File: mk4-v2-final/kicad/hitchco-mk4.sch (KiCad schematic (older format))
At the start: 25 parts, among them J1 Screw_Terminal_01x10, J10 Conn_02x03_Counter_Clockwise, J12 Conn_02x03_Counter_Clockwise, J13 Conn_02x03_Counter_Clockwise, J15 Conn_02x03_Counter_Clockwise, J16 Conn_02x03_Counter_Clockwise, J18 Conn_02x03_Counter_Clockwise, J19 Conn_02x03_Counter_Clockwise, J2 Screw_Terminal_01x10, J21 Conn_02x03_Counter_Clockwise, J22 Conn_02x03_Counter_Clockwise, J24 Conn_02x03_Counter_Clockwise, J25 Conn_02x03_Counter_Clockwise, J26 Conn_02x03_Counter_Clockwise, J27 Conn_02x03_Counter_Clockwise, J28 Conn_02x03_Counter_Clockwise, J30 Conn_02x03_Counter_Clockwise, J4 Screw_Terminal_01x10, J5 Conn_02x03_Counter_Clockwise, J6 Screw_Terminal_01x10, J7 Conn_02x03_Counter_Clockwise, J8 Conn_02x03_Counter_Clockwise

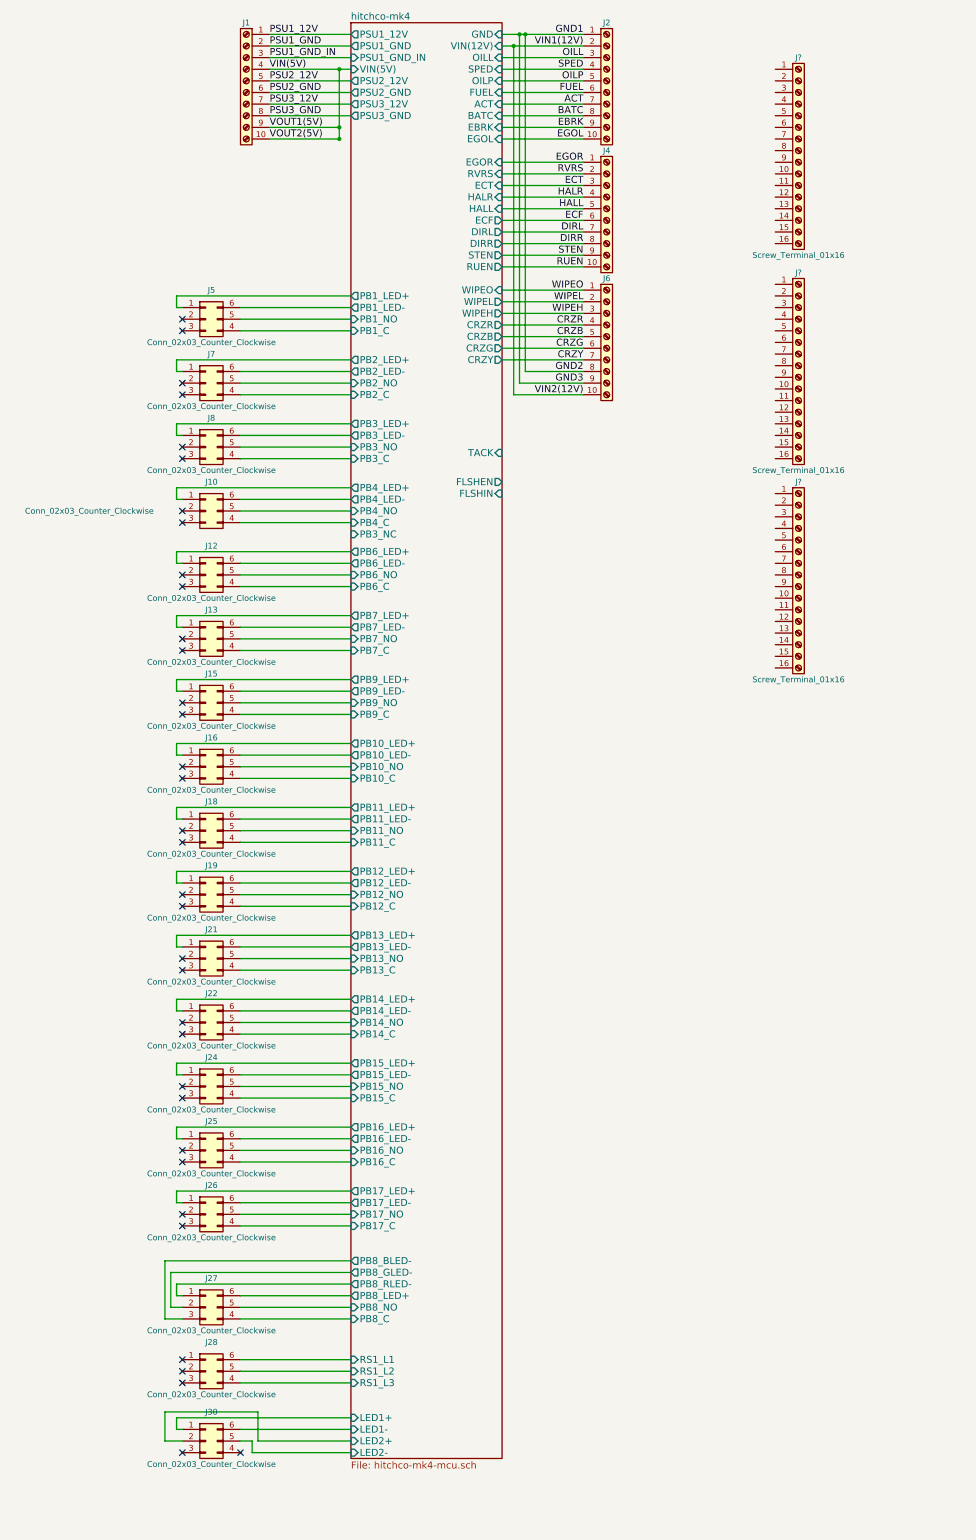
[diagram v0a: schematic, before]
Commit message: got most of the screw terminals planned out in schem
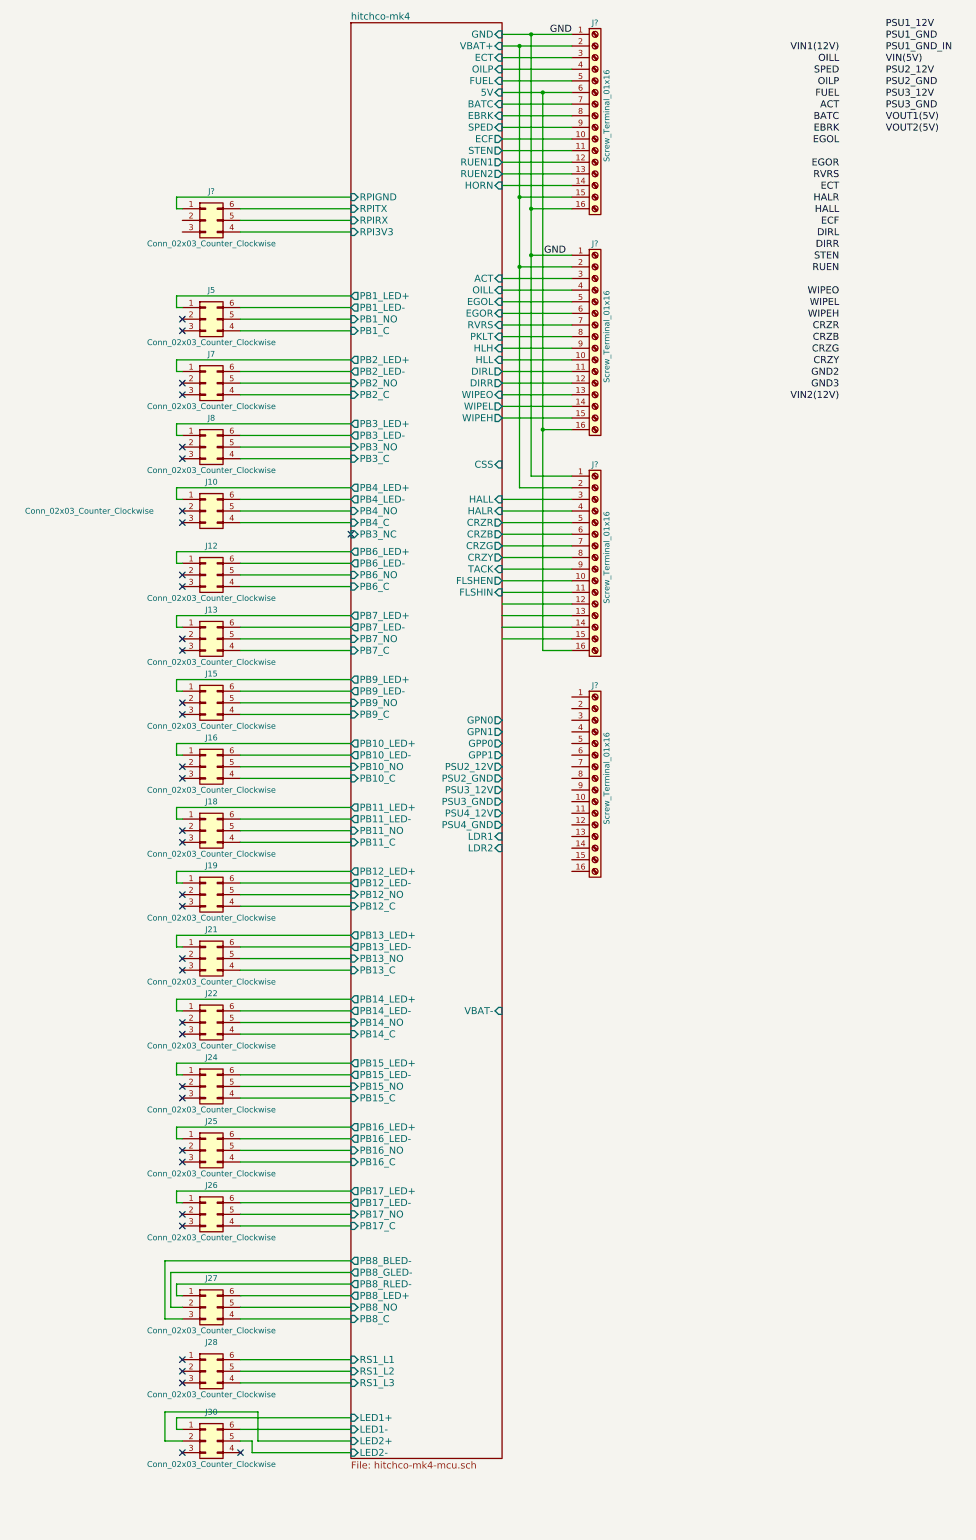
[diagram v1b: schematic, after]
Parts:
- removed J1, J2, J4, J6: Screw_Terminal_01x10, TerminalBlocks_Phoenix:TerminalBlock_Phoenix_MKDS1.5-10pol, symbol Screw_Terminal_01x10
- added J?: Conn_02x03_Counter_Clockwise, Socket_Strips:Socket_Strip_Straight_2x03_Pitch2.54mm, symbol Conn_02x03_Counter_Clockwise
- added J?: Screw_Terminal_01x16, symbol Screw_Terminal_01x16
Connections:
- net hitchco-mk4/FLSHEN: now also J?.10 (Pin_10)
- net hitchco-mk4/FLSHIN: now also J?.11 (Pin_11)
- net hitchco-mk4/TACK: now also J?.9 (Pin_9)
- net GND: now reaches J?.1 (Pin_1)
- net GND: now also J?.1 (Pin_1), J?.1 (Pin_1), J?.16 (Pin_16)
- net hitchco-mk4/ECF: now reaches J?.10 (Pin_10)
- net hitchco-mk4/STEN: now reaches J?.11 (Pin_11)
- net hitchco-mk4/RUEN1: now reaches J?.12 (Pin_12)
- net hitchco-mk4/RUEN2: now reaches J?.13 (Pin_13)
- net hitchco-mk4/HORN: now reaches J?.14 (Pin_14)
- net hitchco-mk4/VBAT+: now reaches J?.15 (Pin_15)
- net hitchco-mk4/VBAT+: now also J?.2 (Pin_2), J?.2 (Pin_2), J?.2 (Pin_2)
- net hitchco-mk4/ECT: now reaches J?.3 (Pin_3)
- net hitchco-mk4/OILP: now reaches J?.4 (Pin_4)
- net hitchco-mk4/FUEL: now reaches J?.5 (Pin_5)
- net hitchco-mk4/5V: now reaches J?.6 (Pin_6)
- net hitchco-mk4/5V: now also J?.16 (Pin_16), J?.16 (Pin_16)
- net hitchco-mk4/BATC: now reaches J?.7 (Pin_7)
- net hitchco-mk4/EBRK: now reaches J?.8 (Pin_8)
- net hitchco-mk4/SPED: now reaches J?.9 (Pin_9)
- net hitchco-mk4/HLL: now reaches J?.10 (Pin_10)
- net hitchco-mk4/DIRL: now reaches J?.11 (Pin_11)
- net hitchco-mk4/DIRR: now reaches J?.12 (Pin_12)
- net hitchco-mk4/WIPEO: now reaches J?.13 (Pin_13)
- net hitchco-mk4/WIPEL: now reaches J?.14 (Pin_14)
- net hitchco-mk4/WIPEH: now reaches J?.15 (Pin_15)
- net hitchco-mk4/ACT: now reaches J?.3 (Pin_3)
- net hitchco-mk4/OILL: now reaches J?.4 (Pin_4)
- net hitchco-mk4/EGOL: now reaches J?.5 (Pin_5)
- net hitchco-mk4/EGOR: now reaches J?.6 (Pin_6)
- net hitchco-mk4/RVRS: now reaches J?.7 (Pin_7)
- net hitchco-mk4/PKLT: now reaches J?.8 (Pin_8)
- net hitchco-mk4/HLH: now reaches J?.9 (Pin_9)
- net hitchco-mk4/HALL: now reaches J?.3 (Pin_3)
- net hitchco-mk4/HALR: now reaches J?.4 (Pin_4)
- net hitchco-mk4/CRZR: now reaches J?.5 (Pin_5)
- net hitchco-mk4/CRZB: now reaches J?.6 (Pin_6)
- net hitchco-mk4/CRZG: now reaches J?.7 (Pin_7)
- net hitchco-mk4/CRZY: now reaches J?.8 (Pin_8)
- new net hitchco-mk4/RPI3V3: J?.4 (Pin_4)
- new net hitchco-mk4/RPIGND: J?.1 (Pin_1)
- new net hitchco-mk4/RPIRX: J?.5 (Pin_5)
- new net hitchco-mk4/RPITX: J?.6 (Pin_6)
- no-connect marks 35 -> 36
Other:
- moved on the sheet: J?

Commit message: added headnight diodes, I don't think software control of them is going to be possible
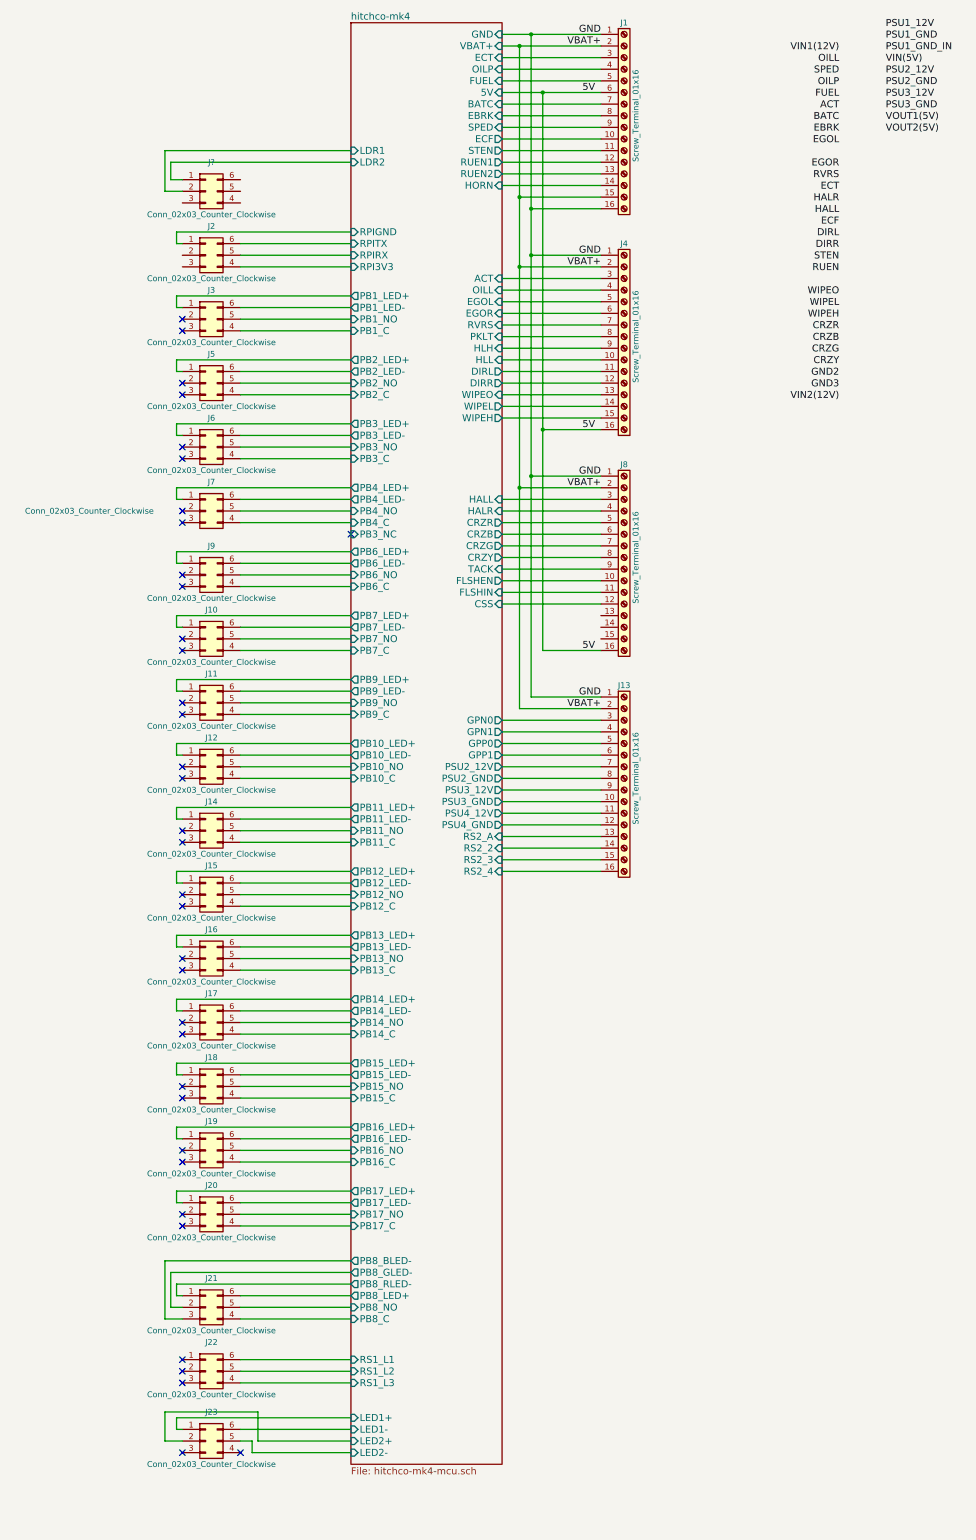
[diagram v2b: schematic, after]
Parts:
- added J?: Conn_02x03_Counter_Clockwise, Socket_Strips:Socket_Strip_Straight_2x03_Pitch2.54mm, symbol Conn_02x03_Counter_Clockwise
- J1, J13, J4, J8: renamed from J?; footprint (none) -> TerminalBlocks_Phoenix:TerminalBlock_Phoenix_MKDS1.5-16pol
- gave numbers to parts that had none: 1
- renumbered J13 to J10, J15 to J11, J16 to J12, J18 to J14, J19 to J15, J21 to J16, J22 to J17, J24 to J18, J25 to J19, J26 to J20, J27 to J21, J28 to J22, J30 to J23, J5 to J3, J7 to J5, J8 to J6, J10 to J7, J12 to J9
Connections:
- net hitchco-mk4/VBAT+ is gone; now on net VBAT+: J1.15 (Pin_15), J1.2 (Pin_2), J4.2 (Pin_2), J8.2 (Pin_2)
- net GND: now also J13.1 (Pin_1)
- net hitchco-mk4/CSS: now also J8.12 (Pin_12)
- net hitchco-mk4/GPN0: now also J13.3 (Pin_3)
- net hitchco-mk4/GPN1: now also J13.4 (Pin_4)
- net hitchco-mk4/GPP0: now also J13.5 (Pin_5)
- net hitchco-mk4/GPP1: now also J13.6 (Pin_6)
- net hitchco-mk4/LDR1: now also J?.2 (Pin_2)
- net hitchco-mk4/LDR2: now also J?.1 (Pin_1)
- net hitchco-mk4/PSU2_12V: now also J13.7 (Pin_7)
- net hitchco-mk4/PSU2_GND: now also J13.8 (Pin_8)
- net hitchco-mk4/PSU3_12V: now also J13.9 (Pin_9)
- net hitchco-mk4/PSU3_GND: now also J13.10 (Pin_10)
- net hitchco-mk4/PSU4_12V: now also J13.11 (Pin_11)
- net hitchco-mk4/PSU4_GND: now also J13.12 (Pin_12)
- net hitchco-mk4/RS2_A: now reaches J13.13 (Pin_13)
- net hitchco-mk4/RS2_2: now reaches J13.14 (Pin_14)
- net hitchco-mk4/RS2_3: now reaches J13.15 (Pin_15)
- net hitchco-mk4/RS2_4: now reaches J13.16 (Pin_16)
- net VBAT+: now reaches J13.2 (Pin_2)
- net hitchco-mk4/5V renamed 5V
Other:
- moved on the sheet: J1, J13, J2, J4, J8

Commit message: schematic is done, footprint association and netlist are also done
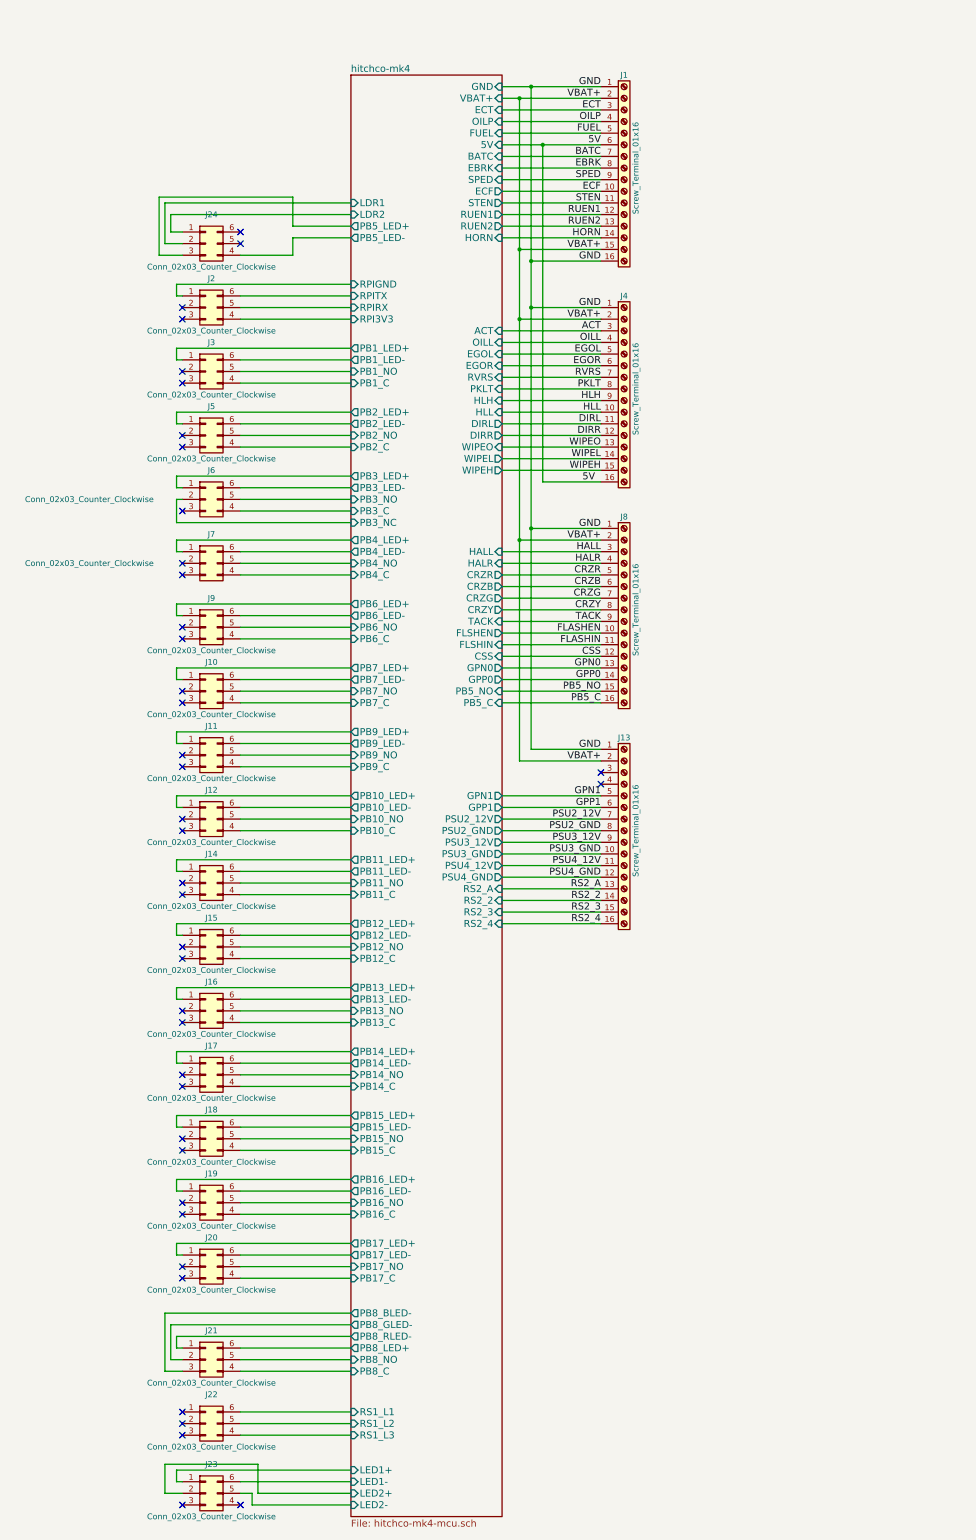
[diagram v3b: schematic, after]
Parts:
- J1, J13, J4, J8: digikey-pn (none) -> 277-13705-ND; mfg-pn (none) -> 1702972
- J10, J11, J12, J14, J15, J16, J17, J18, J19, J2, J20, J21, J22, J23, J5, J6, J7, J9: footprint Socket_Strips:Socket_Strip_Straight_2x03_Pitch2.54mm -> 02x03_shrouded:Shroud_Socket_Strip_Straight_2x03_Pitch2.54mm; digikey-pn (none) -> 609-2845-ND; mfg-pn (none) -> 75869-131LF
- J24: renamed from J?; footprint Socket_Strips:Socket_Strip_Straight_2x03_Pitch2.54mm -> 02x03_shrouded:Shroud_Socket_Strip_Straight_2x03_Pitch2.54mm; digikey-pn (none) -> 609-2845-ND; mfg-pn (none) -> 75869-131LF
- J3: digikey-pn (none) -> 609-2845-ND; mfg-pn (none) -> 75869-131LF
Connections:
- net hitchco-mk4/ACT is gone; now on net ACT: J4.3 (Pin_3)
- net hitchco-mk4/BATC is gone; now on net BATC: J1.7 (Pin_7)
- net hitchco-mk4/CRZB is gone; now on net CRZB: J8.6 (Pin_6)
- net hitchco-mk4/CRZG is gone; now on net CRZG: J8.7 (Pin_7)
- net hitchco-mk4/CRZR is gone; now on net CRZR: J8.5 (Pin_5)
- net hitchco-mk4/CRZY is gone; now on net CRZY: J8.8 (Pin_8)
- net hitchco-mk4/DIRL is gone; now on net DIRL: J4.11 (Pin_11)
- net hitchco-mk4/DIRR is gone; now on net DIRR: J4.12 (Pin_12)
- net hitchco-mk4/EBRK is gone; now on net EBRK: J1.8 (Pin_8)
- net hitchco-mk4/ECF is gone; now on net ECF: J1.10 (Pin_10)
- net hitchco-mk4/ECT is gone; now on net ECT: J1.3 (Pin_3)
- net hitchco-mk4/EGOL is gone; now on net EGOL: J4.5 (Pin_5)
- net hitchco-mk4/EGOR is gone; now on net EGOR: J4.6 (Pin_6)
- net hitchco-mk4/FUEL is gone; now on net FUEL: J1.5 (Pin_5)
- net hitchco-mk4/HALL is gone; now on net HALL: J8.3 (Pin_3)
- net hitchco-mk4/HALR is gone; now on net HALR: J8.4 (Pin_4)
- net hitchco-mk4/OILL is gone; now on net OILL: J4.4 (Pin_4)
- net hitchco-mk4/OILP is gone; now on net OILP: J1.4 (Pin_4)
- net hitchco-mk4/PSU2_12V is gone; now on net PSU2_12V: J13.7 (Pin_7)
- net hitchco-mk4/PSU2_GND is gone; now on net PSU2_GND: J13.8 (Pin_8)
- net hitchco-mk4/PSU3_12V is gone; now on net PSU3_12V: J13.9 (Pin_9)
- net hitchco-mk4/PSU3_GND is gone; now on net PSU3_GND: J13.10 (Pin_10)
- net hitchco-mk4/RVRS is gone; now on net RVRS: J4.7 (Pin_7)
- net hitchco-mk4/SPED is gone; now on net SPED: J1.9 (Pin_9)
- net hitchco-mk4/STEN is gone; now on net STEN: J1.11 (Pin_11)
- net hitchco-mk4/WIPEH is gone; now on net WIPEH: J4.15 (Pin_15)
- net hitchco-mk4/WIPEL is gone; now on net WIPEL: J4.14 (Pin_14)
- net hitchco-mk4/WIPEO is gone; now on net WIPEO: J4.13 (Pin_13)
- net 5V: no longer J8.16 (Pin_16)
- net hitchco-mk4/PB3_NC: now also J6.2 (Pin_2)
- net GPN0: now reaches J8.13 (Pin_13)
- net GPP0: now reaches J8.14 (Pin_14)
- net PB5_NO: now reaches J8.15 (Pin_15)
- net hitchco-mk4/PB5_LED+: now reaches J24.3 (Pin_3)
- net hitchco-mk4/PB5_LED-: now reaches J24.4 (Pin_4)
- net hitchco-mk4/CSS renamed CSS
- net hitchco-mk4/FLSHEN renamed FLASHEN
- net hitchco-mk4/FLSHIN renamed FLASHIN
- net hitchco-mk4/GPN0: no longer names the net of J13.3 (Pin_3)
- net hitchco-mk4/GPN1: no longer names the net of J13.4 (Pin_4)
- net hitchco-mk4/GPP0 renamed GPN1
- net hitchco-mk4/GPP1 renamed GPP1
- net hitchco-mk4/HLH renamed HLH
- net hitchco-mk4/HLL renamed HLL
- net hitchco-mk4/HORN renamed HORN
- net hitchco-mk4/PKLT renamed PKLT
- net hitchco-mk4/PSU4_12V renamed PSU4_12V
- net hitchco-mk4/PSU4_GND renamed PSU4_GND
- net hitchco-mk4/RS2_2 renamed RS2_2
- net hitchco-mk4/RS2_3 renamed RS2_3
- net hitchco-mk4/RS2_4 renamed RS2_4
- net hitchco-mk4/RS2_A renamed RS2_A
- net hitchco-mk4/RUEN1 renamed RUEN1
- net hitchco-mk4/RUEN2 renamed RUEN2
- net hitchco-mk4/TACK renamed TACK
- new net PB5_C: J8.16 (Pin_16)
- no-connect marks 36 -> 40
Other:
- moved on the sheet: J1, J10, J11, J12, J13, J14, J15, J16, J17, J18, J19, J2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
